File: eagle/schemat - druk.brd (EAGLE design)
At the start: 162 parts, among them IC1 MEGA8-AI, IC2 MEGA8-AI, IC3 MEGA8-AI, IC4 MEGA8-AI, IC5 MEGA8-AI, IC6 MEGA8-AI, Q1 N-MOSFET BSS138, Q10 N-MOSFET BSS138, Q11 N-MOSFET BSS138, Q12 N-MOSFET BSS138, Q2 N-MOSFET BSS138, Q3 N-MOSFET BSS138, Q4 N-MOSFET BSS138, Q5 N-MOSFET BSS138, Q6 N-MOSFET BSS138, Q7 N-MOSFET BSS138, Q8 N-MOSFET BSS138, Q9 N-MOSFET BSS138, U1 LCD-16X2SILK, U2 LCD-16X2SILK, U3 LCD-16X2SILK, U4 LCD-16X2SILK, U5 LCD-16X2SILK, U6 LCD-16X2SILK, X10 MINI-USB-32005-301, X12 MINI-USB-32005-301, X2 MINI-USB-32005-301, X4 MINI-USB-32005-301, X6 MINI-USB-32005-301, X8 MINI-USB-32005-301, Y1 16MHz, Y2 16MHz, Y3 16MHz, Y4 16MHz, Y5 16MHz, Y6 16MHz

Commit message: Schemat do druku
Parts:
- removed X10, X12, X8: MINI-USB-32005-301, con-cypressindustries:32005-301
- removed X11, X7, X9: (no value), con-ptr500:AK300/6
- added GND, GND1, GND2, GND3, GND4, GND5, MIESZANIE_GND, MIESZANIE_GND1, MIESZANIE_GND2, MIESZANIE_GND3, MIESZANIE_GND4, MIESZANIE_GND5, MISO, MISO1, MISO2, MISO3, MISO4, MISO5, MOSI, MOSI1, MOSI2, MOSI3, MOSI4, MOSI5, RESET, RESET1, RESET2, RESET3, RESET4, RESET5, SCK, SCK1, SCK2, SCK3, SCK4, SCK5, TEMP_GND, TEMP_GND1, TEMP_GND2, TEMP_GND3, TEMP_GND4, TEMP_GND5, VCC, VCC1, VCC2, VCC3, VCC4, VCC5, ZAPISZ_GND, ZAPISZ_GND1, ZAPISZ_GND2, ZAPISZ_GND3, ZAPISZ_GND4, ZAPISZ_GND5: M01NOSILK-KIT, SparkFun-Connectors:1X01NS-KIT
- MIESZANIE, MIESZANIE1, MIESZANIE2, MIESZANIE3, MIESZANIE4, MIESZANIE5, TEMP, TEMP1, TEMP2, TEMP3, TEMP4, TEMP5, ZAPISZ, ZAPISZ1, ZAPISZ2, ZAPISZ3, ZAPISZ4, ZAPISZ5: value M02PTH -> M01NOSILK-KIT; device SparkFun-Connectors:1X02 -> SparkFun-Connectors:1X01NS-KIT
- X2, X4, X6: value MINI-USB-32005-301 -> (none); device con-cypressindustries:32005-301 -> con-ptr500:AK300/6
- moved X3 114.3 mm to (68.7, 42.9)
- moved X6 95.9 mm to (170.7, -9.65), flipped to the top
- moved X2 90.9 mm to (170.4, 95.1), flipped to the top
- moved X5 52.5 mm to (68.8, -9.53)
- moved X4 36.8 mm to (170.6, 42.8), flipped to the top
- moved TEMP_PRZEKAZNIK15 2.75 mm to (172.1, -14.7)
- moved TEMP_PRZEKAZNIK12 2.57 mm to (70.2, -14.6)
- moved TEMP_PRZEKAZNIK9 1.98 mm to (172.0, 37.7)
- moved TEMP_PRZEKAZNIK3 1.89 mm to (171.8, 90.0)
- moved TEMP_PRZEKAZNIK6 1.80 mm to (70.1, 37.8)
- moved TEMP_PRZEKAZNIK 1.71 mm to (70.0, 90.2)
- moved MIESZANIE_PRZEKAZNIK5 1.69 mm to (178.2, -14.7)
- moved MIESZANIE_PRZEKAZNIK4 1.55 mm to (76.3, -14.6)
- moved C30 1.45 mm to (160.5, -25.5)
- moved C25 1.30 mm to (58.7, -25.4)
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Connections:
- removed net N$1 (its old number): IC1.29, R1.1
- removed net N$19 (its old number): TEMP_PRZEKAZNIK3.1, X3.3
- removed net N$20 (its old number): MIESZANIE_PRZEKAZNIK1.1, X3.5
- removed net N$21 (its old number): IC3.29, R5.1
- removed net N$29 (its old number): TEMP_PRZEKAZNIK6.1, X5.3
- removed net N$30 (its old number): MIESZANIE_PRZEKAZNIK2.1, X5.5
- removed net N$31 (its old number): IC4.29, R7.1
- removed net N$39 (its old number): TEMP_PRZEKAZNIK9.1, X7.3
- removed net N$40 (its old number): MIESZANIE_PRZEKAZNIK3.1, X7.5
- removed net N$41 (its old number): IC5.29, R9.1
- removed net N$49 (its old number): TEMP_PRZEKAZNIK12.1, X9.3
- removed net N$50 (its old number): MIESZANIE_PRZEKAZNIK4.1, X9.5
- removed net N$51 (its old number): IC6.29, R11.1
- removed net N$59: TEMP_PRZEKAZNIK15.1, X11.3
- removed net N$60: MIESZANIE_PRZEKAZNIK5.1, X11.5
- removed net N$8 (its old number): IC2.29, R3.1
- new net N$17: TEMP_PRZEKAZNIK3.1, X2.3
- new net N$18: MIESZANIE_PRZEKAZNIK1.1, X2.5
- new net N$26: TEMP_PRZEKAZNIK6.1, X3.3
- new net N$27: MIESZANIE_PRZEKAZNIK2.1, X3.5
- new net N$35: TEMP_PRZEKAZNIK9.1, X4.3
- new net N$36: MIESZANIE_PRZEKAZNIK3.1, X4.5
- new net N$44: TEMP_PRZEKAZNIK12.1, X5.3
- new net N$45: MIESZANIE_PRZEKAZNIK4.1, X5.5
- new net N$53: TEMP_PRZEKAZNIK15.1, X6.3
- new net N$54: MIESZANIE_PRZEKAZNIK5.1, X6.5
- new net RESET: IC1.29, R1.1, RESET.1
- new net RESET1: IC2.29, R3.1, RESET1.1
- new net RESET2: IC3.29, R5.1, RESET2.1
- new net RESET3: IC4.29, R7.1, RESET3.1
- new net RESET4: IC5.29, R9.1, RESET4.1
- new net RESET5: IC6.29, R11.1, RESET5.1
- net +5V: now also VCC.1; no longer X2.1
- net +5V1: now also VCC1.1; no longer X4.1
- net +5V2: now also VCC2.1; no longer X6.1
- net +5V3: now also VCC3.1; no longer X8.1
- net +5V4: now also VCC4.1; no longer X10.1
- net +5V5: now also VCC5.1; no longer X12.1
- net AGND1: now also X2.2, X2.4, X2.6; no longer X3.2, X3.4, X3.6
- net AGND2: now also X3.2, X3.4, X3.6; no longer X5.2, X5.4, X5.6
- net AGND3: now also X4.2, X4.4, X4.6; no longer X7.2, X7.4, X7.6
- net AGND4: now also X5.2, X5.4, X5.6; no longer X9.2, X9.4, X9.6
- net AGND5: now also X6.2, X6.4, X6.6; no longer X11.2, X11.4, X11.6
- net GND: now also GND.1, MIESZANIE_GND.1, TEMP_GND.1, ZAPISZ_GND.1; no longer MIESZANIE.2, TEMP.2, X2.5, ZAPISZ.2
- net GND1: now also GND1.1, MIESZANIE_GND1.1, TEMP_GND1.1, ZAPISZ_GND1.1; no longer MIESZANIE1.2, TEMP1.2, X4.5, ZAPISZ1.2
- net GND2: now also GND2.1, MIESZANIE_GND2.1, TEMP_GND2.1, ZAPISZ_GND2.1; no longer MIESZANIE2.2, TEMP2.2, X6.5, ZAPISZ2.2
- net GND3: now also GND3.1, MIESZANIE_GND3.1, TEMP_GND3.1, ZAPISZ_GND3.1; no longer MIESZANIE3.2, TEMP3.2, X8.5, ZAPISZ3.2
- net GND4: now also GND4.1, MIESZANIE_GND4.1, TEMP_GND4.1, ZAPISZ_GND4.1; no longer MIESZANIE4.2, TEMP4.2, X10.5, ZAPISZ4.2
- net GND5: now also GND5.1, MIESZANIE_GND5.1, TEMP_GND5.1, ZAPISZ_GND5.1; no longer MIESZANIE5.2, TEMP5.2, X12.5, ZAPISZ5.2
- net MISO: now also MISO.1; no longer X2.3
- net MISO1: now also MISO1.1; no longer X4.3
- net MISO2: now also MISO2.1; no longer X6.3
- net MISO3: now also MISO3.1; no longer X8.3
- net MISO4: now also MISO4.1; no longer X10.3
- net MISO5: now also MISO5.1; no longer X12.3
- net MOSI: now also MOSI.1; no longer X2.2
- net MOSI1: now also MOSI1.1; no longer X4.2
- net MOSI2: now also MOSI2.1; no longer X6.2
- net MOSI3: now also MOSI3.1; no longer X8.2
- net MOSI4: now also MOSI4.1; no longer X10.2
- net MOSI5: now also MOSI5.1; no longer X12.2
- net SCK: now also SCK.1; no longer X2.4
- net SCK1: now also SCK1.1; no longer X4.4
- net SCK2: now also SCK2.1; no longer X6.4
- net SCK3: now also SCK3.1; no longer X8.4
- net SCK4: now also SCK4.1; no longer X10.4
- net SCK5: now also SCK5.1; no longer X12.4
- net VDD1: now also X2.1; no longer X3.1
- net VDD2: now also X3.1; no longer X5.1
- net VDD3: now also X4.1; no longer X7.1
- net VDD4: now also X5.1; no longer X9.1
- net VDD5: now also X6.1; no longer X11.1
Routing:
- net +5V1: track 387.2 -> 354.1 mm
- net +5V5: track 387.2 -> 354.1 mm
- net +5V4: track 387.2 -> 354.1 mm
- net +5V: track 387.2 -> 354.1 mm
- net +5V2: track 387.2 -> 354.1 mm
- net +5V3: track 387.2 -> 354.1 mm
- net RESET3: track 0.00 -> 13.0 mm
- net RESET4: track 0.00 -> 13.0 mm
- net RESET2: track 0.00 -> 13.0 mm
- net RESET1: track 0.00 -> 13.0 mm
- net RESET: track 0.00 -> 13.0 mm
- net RESET5: track 0.00 -> 13.0 mm
- net N$41 (its old number): track 8.63 -> 0.00 mm
- net N$21 (its old number): track 8.63 -> 0.00 mm
- net N$1 (its old number): track 8.63 -> 0.00 mm
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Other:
- board text added: "+5V"
- board text added: "GND"
- board text added: "MIESZ"
- board text added: "MIESZANIE"
- board text added: "MISO"
- board text added: "MOSI"
- board text added: "Marcin Twardak 07-02-2014"
- board text added: "Niepodłączone"
- board text added: "P+"
- board text added: "P-"
- board text added: "RST"
- board text added: "SCK"
- board text added: "TEMP"
- board text added: "VCC"
- board text added: "ZAPISZ"
- board text added: "ZAPISZ-GND"

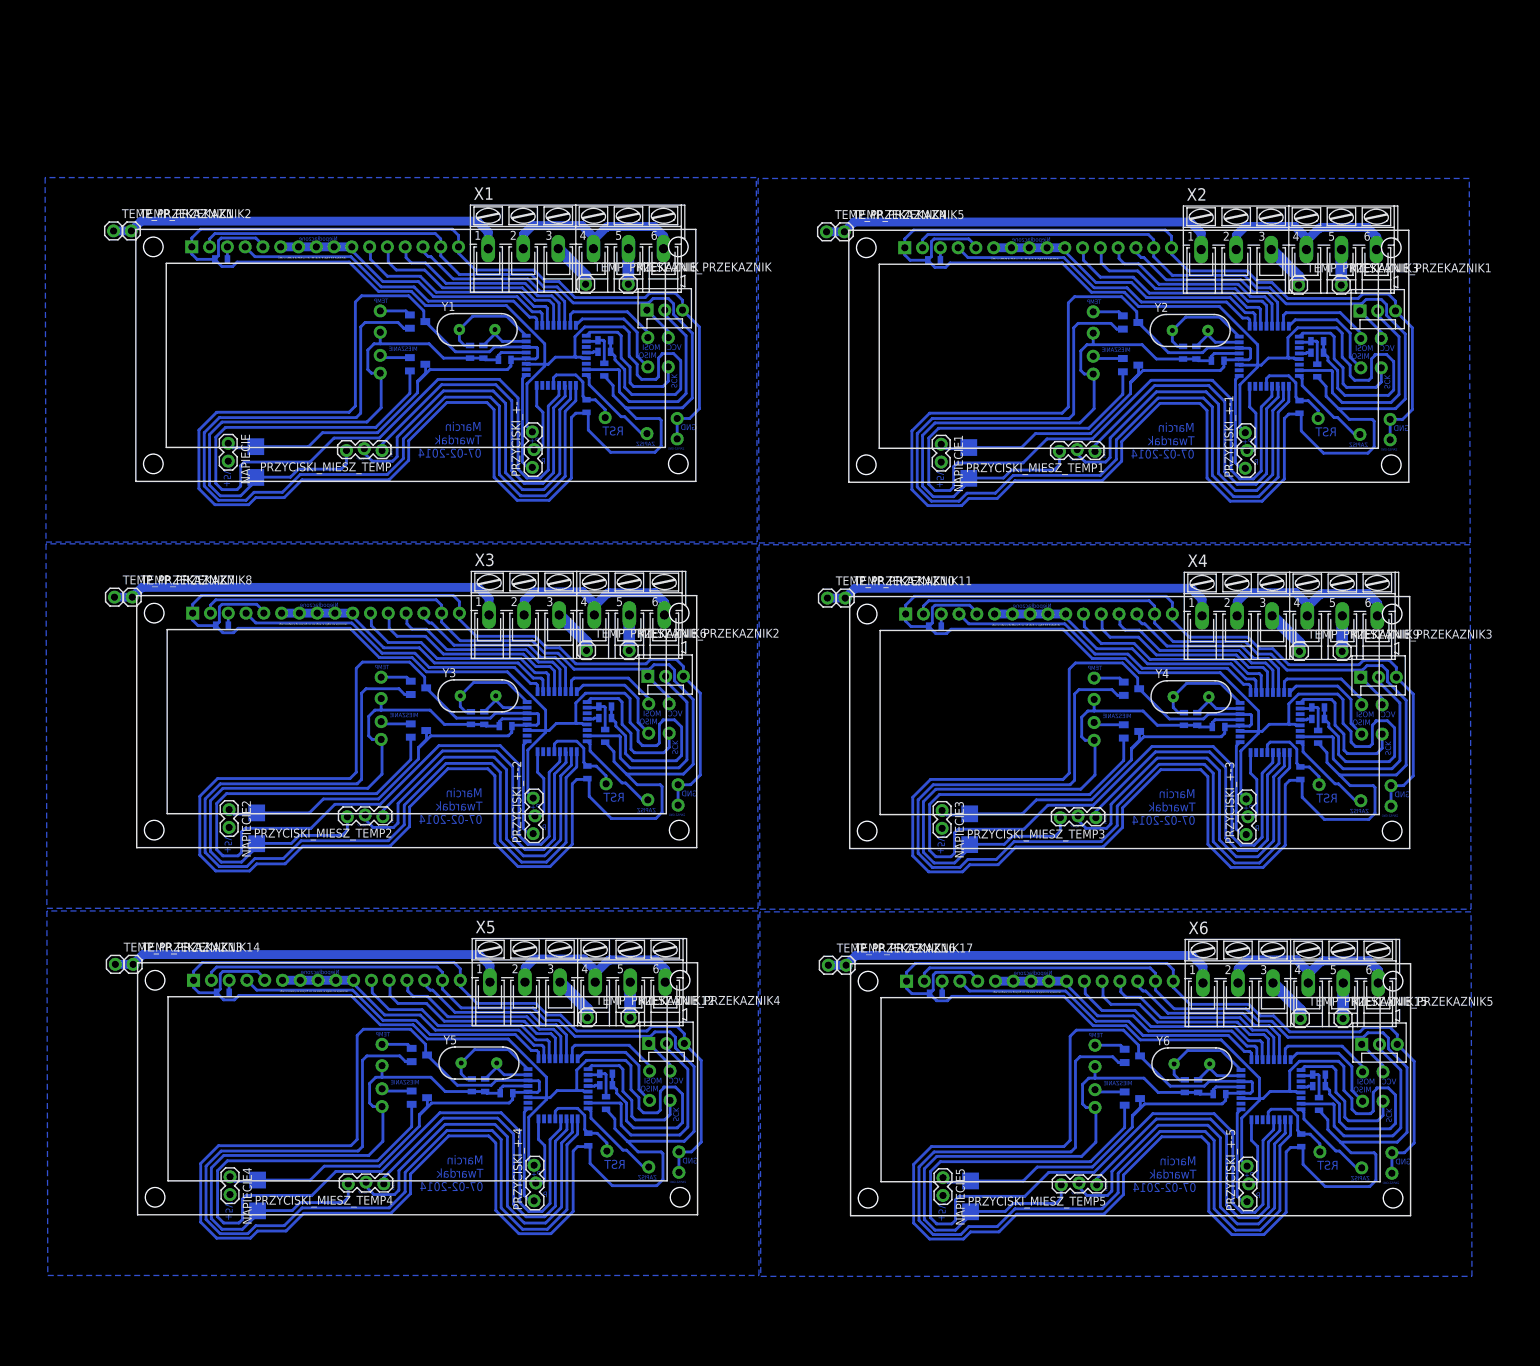
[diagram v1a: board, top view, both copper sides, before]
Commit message: Dodane opisy + wersja do druku
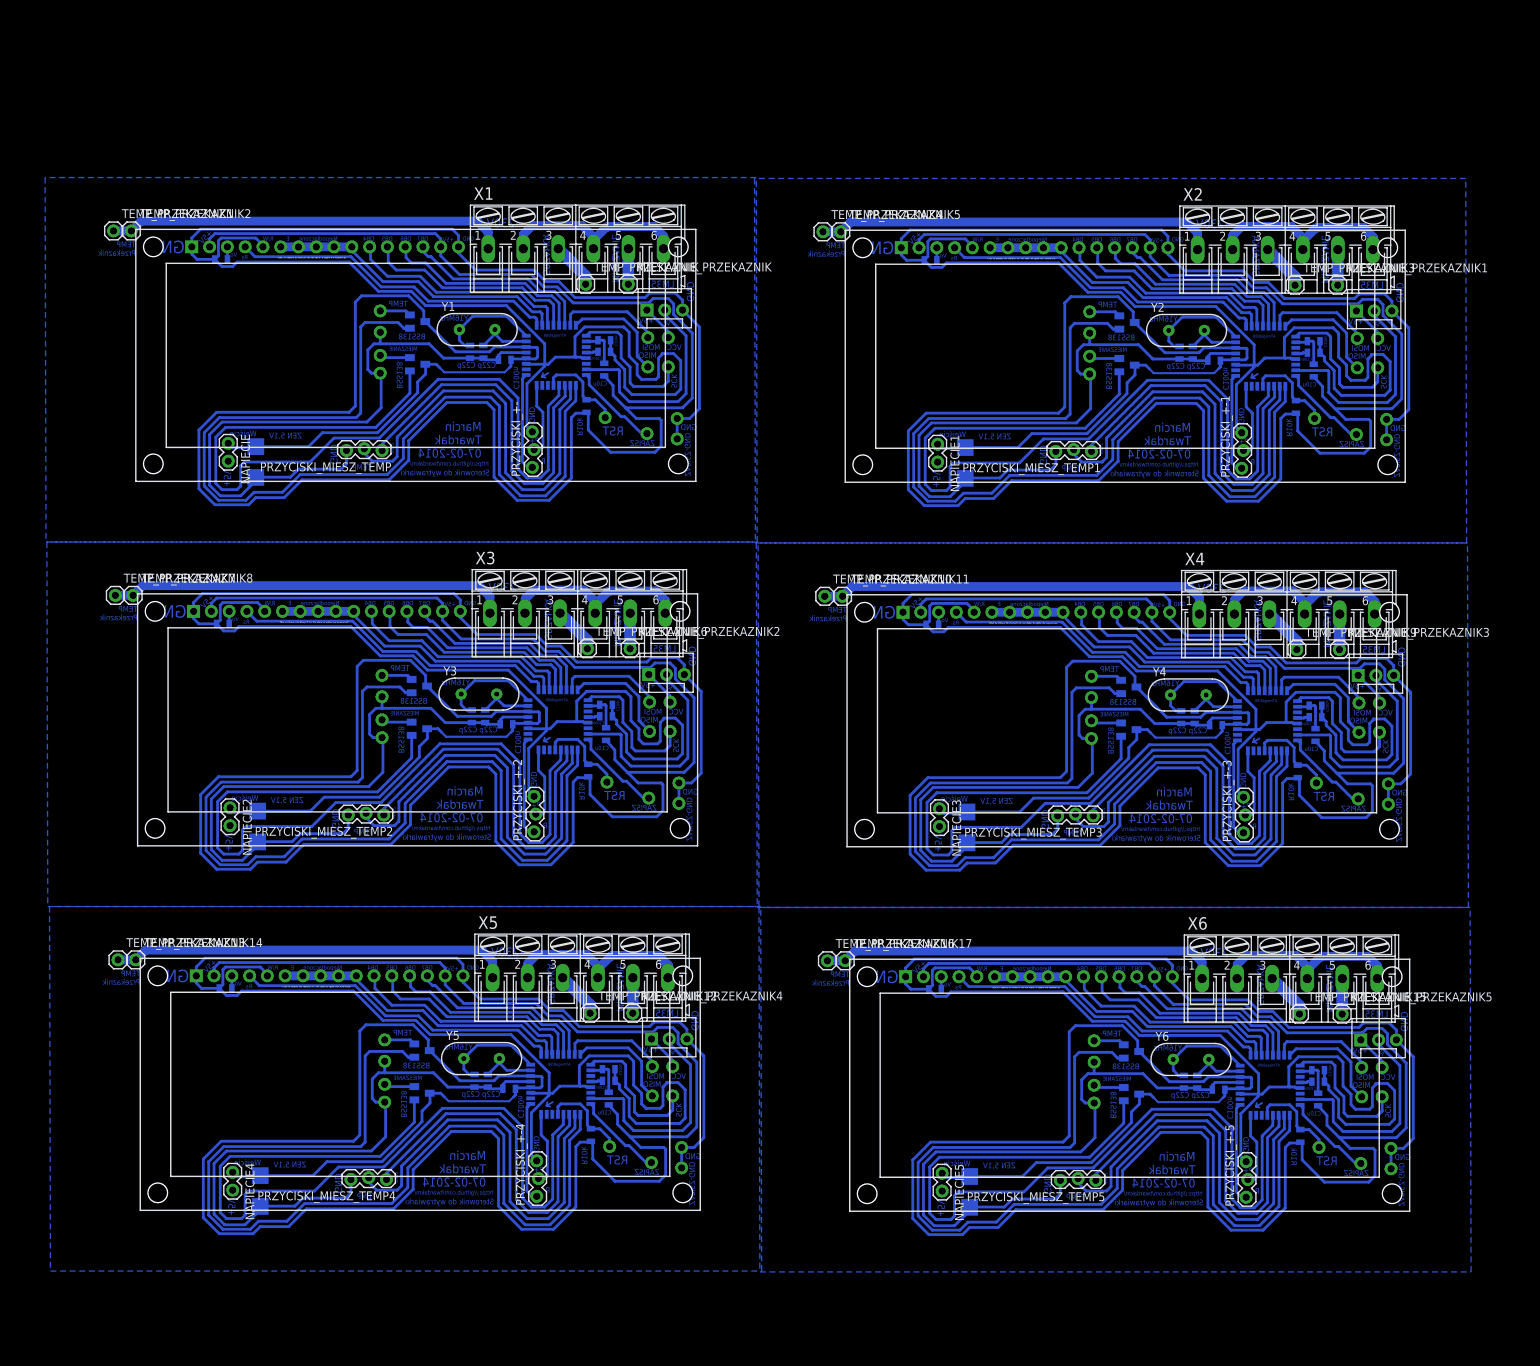
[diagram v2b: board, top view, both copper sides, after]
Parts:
- moved PRZYCISKI_+-4 0.74 mm to (63.1, -40.1)
- moved U$5 0.74 mm to (23.5, -39.4)
- moved ZAPISZ4 0.74 mm to (79.4, -35.3)
- moved ZAPISZ_GND4 0.74 mm to (83.7, -36.1)
- moved C21 0.74 mm to (73.3, -23.6)
- moved C22 0.74 mm to (73.3, -22.0)
- moved C23 0.74 mm to (56.0, -23.6)
- moved C24 0.74 mm to (54.1, -23.6)
- moved IC5 0.74 mm to (66.4, -24.1)
- moved L5 0.74 mm to (73.3, -26.2)
- moved LM4 0.74 mm to (79.4, -17.7)
- moved MIESZANIE4 0.74 mm to (41.3, -24.1)
- moved MISO4 0.74 mm to (79.5, -25.8)
- moved MOSI4 0.74 mm to (79.5, -21.6)
- moved Q10 0.74 mm to (46.6, -25.4)
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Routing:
- net N$20: track 0.00 -> 2.07 mm
- net N$50: track 0.00 -> 2.07 mm
- net N$30: track 0.00 -> 2.07 mm
- net N$1: track 0.00 -> 2.07 mm
- net N$60: track 0.00 -> 2.07 mm
- net N$40: track 0.00 -> 2.07 mm
- net +5V3: track 354.1 -> 352.9 mm
- net +5V2: track 354.1 -> 352.9 mm
- net +5V1: track 354.1 -> 352.9 mm
- net +5V4: track 354.1 -> 352.9 mm
- net +5V: track 354.1 -> 352.9 mm
- net +5V5: track 354.1 -> 352.9 mm
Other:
- board text added: "ADC"
- board text added: "ATmega8/88"
- board text added: "BSS138"
- board text added: "C100n"
- board text added: "C10u"
- board text added: "C22p"
- board text added: "DB4"
- board text added: "DB5"
- board text added: "DB6"
- board text added: "DB7"
- board text added: "E"
- board text added: "GRZAŁKA"
- board text added: "LM35"
- board text added: "R/W"
- board text added: "R10k"
- board text added: "Rs"
- board text added: "Sterownik do wytrawiarki"
- board text added: "TEMP Przekaznik"
- board text added: "Vo"
- board text added: "Wejście"
- board text added: "Y16MHz"
- board text added: "ZEN 5,1V"
- board text added: "https://github.com/twardakm/"
- board text added: "~230V"

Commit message: kolejne poprawki
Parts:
- moved IC2 0.77 mm to (167.9, 80.0)
- moved MIESZANIE1 0.77 mm to (142.7, 80.0)
- moved RESET1 0.77 mm to (174.9, 71.1)
- moved TEMP_PRZEKAZNIK4 0.77 mm to (104.6, 97.8)
- moved TEMP_PRZEKAZNIK5 0.77 mm to (107.2, 97.8)
- moved U2 0.77 mm to (147.8, 80.0)
- moved ZAPISZ1 0.77 mm to (180.8, 68.8)
- moved ZAPISZ_GND1 0.77 mm to (185.2, 68.1)
- moved C10 0.77 mm to (160.5, 79.4)
- moved C6 0.77 mm to (174.8, 80.5)
- moved C7 0.77 mm to (174.8, 82.2)
- moved C8 0.77 mm to (157.5, 80.5)
- moved C9 0.77 mm to (155.6, 80.5)
- moved GND1 0.77 mm to (185.2, 71.0)
- moved L2 0.77 mm to (174.8, 78.0)
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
